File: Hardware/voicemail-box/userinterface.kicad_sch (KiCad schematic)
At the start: 5 parts, among them SW801 Push_Button

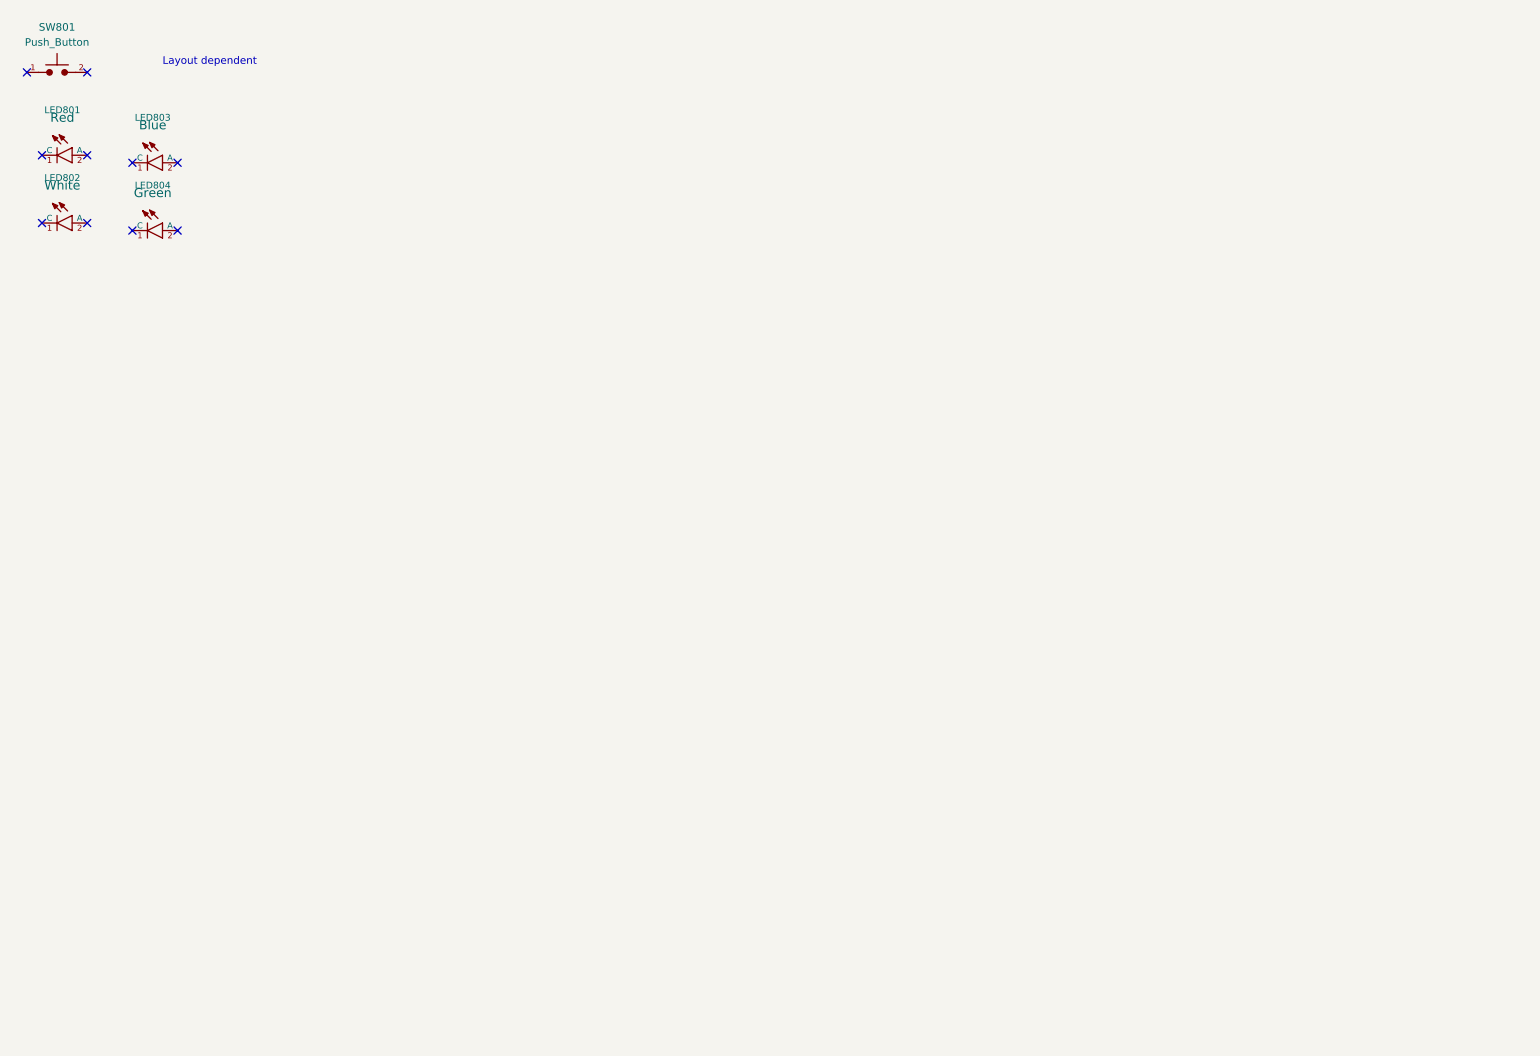
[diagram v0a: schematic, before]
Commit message: HW Layout progress todo: + Antenna + Audio Jacks + Planes (Supply only)
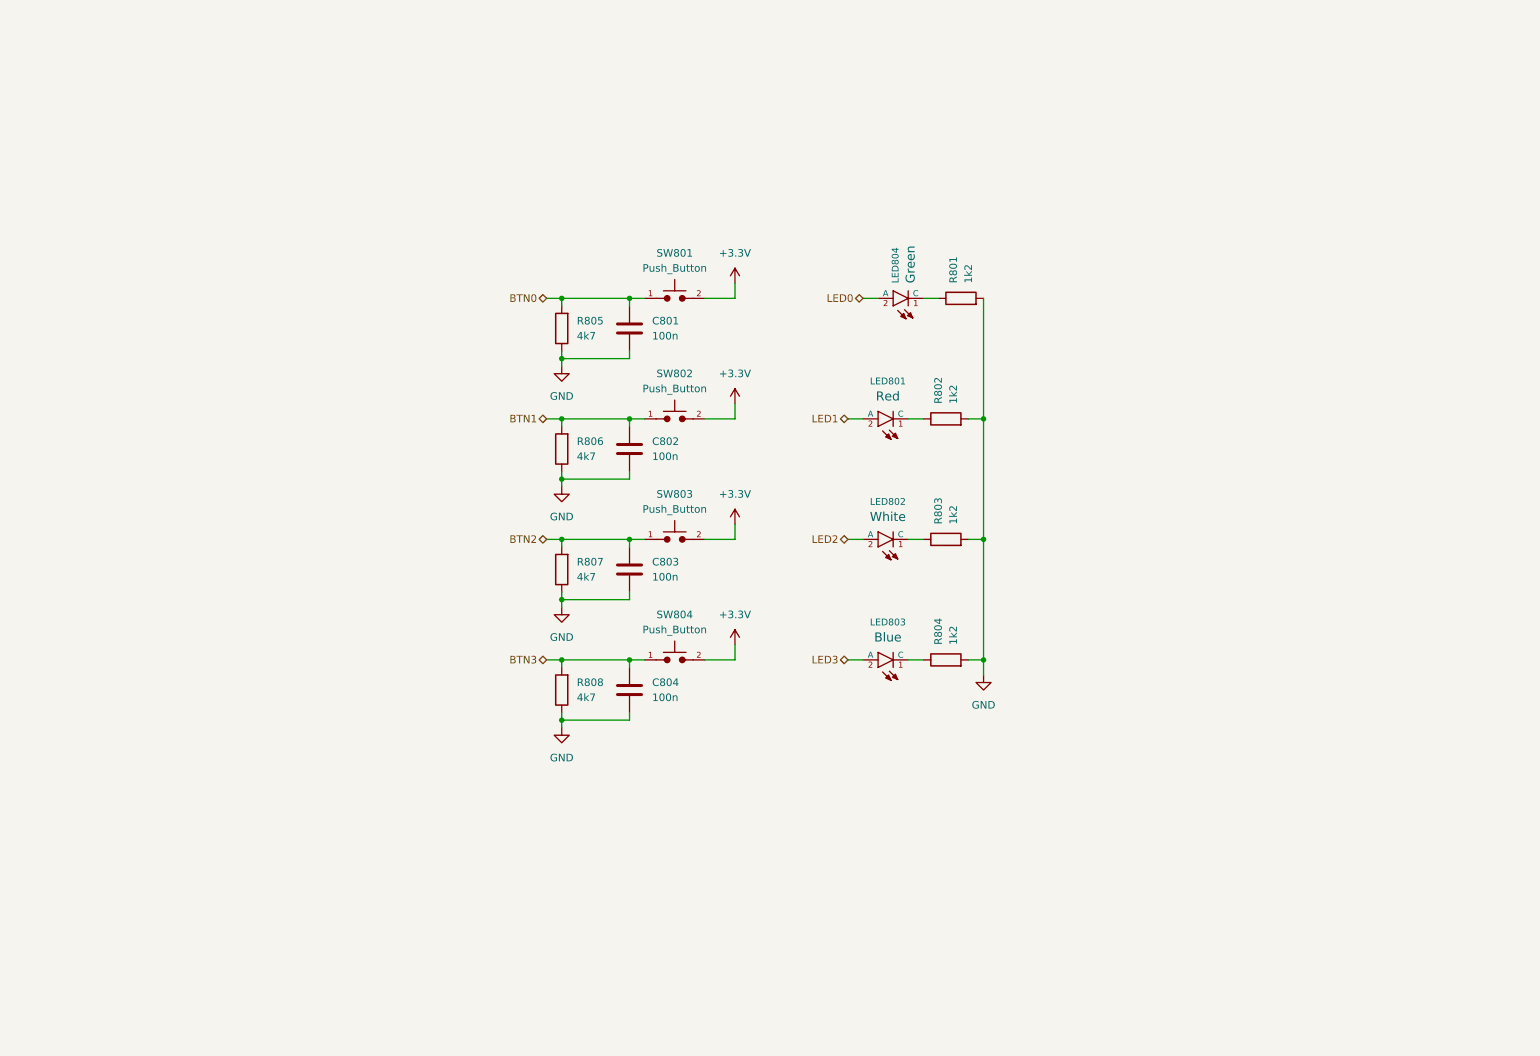
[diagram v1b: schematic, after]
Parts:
- added C801, C802, C803, C804: 100n, Capacitor_SMD:C_0603_1608Metric_Pad1.08x0.95mm_HandSolder, symbol Device:C
- added R801, R802, R803, R804: 1k2, Resistor_SMD:R_0603_1608Metric_Pad0.98x0.95mm_HandSolder, symbol Device:R
- added R805, R806, R807, R808: 4k7, Resistor_SMD:R_0603_1608Metric_Pad0.98x0.95mm_HandSolder, symbol Device:R
- added SW802, SW803, SW804: Push_Button, Button_Switch_THT:SW_PUSH_6mm, symbol PCM_SL_Devices:Push_Button
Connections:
- net BTN0: now reaches SW801.1
- net BTN0: now also C801.1, R805.2
- net +3.3V: now reaches SW801.2
- net +3.3V: now also SW802.2, SW803.2, SW804.2
- net at LED801.1 (C): now also R802.1
- net LED1: now reaches LED801.2 (A)
- net at LED802.1 (C): now also R803.1
- net LED2: now reaches LED802.2 (A)
- net at LED803.1 (C): now also R804.1
- net LED3: now reaches LED803.2 (A)
- net at LED804.1 (C): now also R801.1
- net LED0: now reaches LED804.2 (A)
- new net BTN1: C802.1, R806.2, SW802.1
- new net BTN2: C803.1, R807.2, SW803.1
- new net BTN3: C804.1, R808.2, SW804.1
- new net GND: C801.2, C802.2, C803.2, C804.2, R801.2, R802.2, R803.2, R804.2, R805.1, R806.1, R807.1, R808.1
- no-connect marks 10 -> 0
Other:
- note removed: "Layout dependent"
- moved on the sheet: LED801, LED802, LED803, LED804, SW801

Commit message: layout progress step
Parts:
- added J801: Conn_01x08, Connector_PinHeader_2.54mm:PinHeader_1x08_P2.54mm_Vertical, symbol Connector_Generic:Conn_01x08
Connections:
- net +3.3V: now also J801.1 (Pin_1)
- net BTN1: now also J801.2 (Pin_2)
- net BTN2: now also J801.4 (Pin_4)
- net BTN3: now also J801.6 (Pin_6)
- net GND: now also J801.8 (Pin_8)
- net LED1: now also J801.3 (Pin_3)
- net LED2: now also J801.5 (Pin_5)
- net LED3: now also J801.7 (Pin_7)
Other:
- moved on the sheet: C801, C802, C803, C804, LED801, LED802, LED803, LED804, R801, R802, R803, R804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

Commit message: schema review
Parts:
- removed LED802: White_min200mcd_0603, PCM_4ms_LED:LED_0603_1608Metric, symbol PCM_4ms_LED:White_min200mcd_0603
- removed LED803: Blue_56mcd_0603, PCM_4ms_LED:LED_0603_1608Metric, symbol PCM_4ms_LED:Blue_56mcd_0603
- removed R803, R804: 1k2, Resistor_SMD:R_0603_1608Metric_Pad0.98x0.95mm_HandSolder, symbol Device:R
- added C811: 100n, Capacitor_SMD:C_0603_1608Metric_Pad1.08x0.95mm_HandSolder, symbol Device:C
- added J802, J803: Conn_01x03, Connector_PinHeader_2.54mm:PinHeader_1x03_P2.54mm_Vertical, symbol Connector_Generic:Conn_01x03
- added R809, R810, R811, R812, R813, R814: 4k7, Resistor_SMD:R_0603_1608Metric_Pad0.98x0.95mm_HandSolder, symbol Device:R
- added RV801, RV802: potentiometer_RK163, Potentiometer_THT:Potentiometer_Alps_RK163_Single_Horizontal, symbol PCM_SL_Devices:potentiometer_RK163
- added U801: 74LS07, Package_SO:SOIC-14_3.9x8.7mm_P1.27mm, symbol 74xx:74LS07
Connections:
- net +3.3V: now also J802.1 (Pin_1), J803.1 (Pin_1), RV801.1, RV802.1; no longer J801.1 (Pin_1), SW801.2, SW802.2, SW803.2, SW804.2
- net BTN0: now also U801.6; no longer SW801.1
- net BTN1: now also U801.8; no longer J801.2 (Pin_2), SW802.1
- net BTN2: now also U801.10; no longer J801.4 (Pin_4), SW803.1
- net BTN3: now also U801.12; no longer J801.6 (Pin_6), SW804.1
- net GND: now also SW801.2, SW802.2, SW803.2, SW804.2, C811.2, J802.3 (Pin_3), J803.3 (Pin_3), R809.1, R810.1, RV801.3, RV802.3, U801.7 (GND); no longer R801.2, R802.2
- net LED0: now also R810.2, U801.1; no longer LED804.2 (A)
- net LED1: now also R809.2, U801.3; no longer J801.3 (Pin_3), LED801.2 (A)
- net LED2 renamed ext_BTN1
- net ext_BTN1: now also SW802.1, R811.1, U801.9
- net LED3 renamed ext_BTN3
- net ext_BTN3: now also SW804.1, R813.1, U801.13
- new net +5V: C811.1, J801.1 (Pin_1), LED801.2 (A), LED804.2 (A), R811.2, R812.2, R813.2, R814.2, U801.14 (VCC)
- new net POT1: J802.2 (Pin_2), RV801.2
- new net POT2: J803.2 (Pin_2), RV802.2
- new net ext_BTN0: J801.4 (Pin_4), R814.1, SW801.1, U801.5
- new net ext_BTN2: J801.6 (Pin_6), R812.1, SW803.1, U801.11
- new net ext_LED1: J801.2 (Pin_2), R801.2, U801.2
- new net ext_LED2: J801.3 (Pin_3), R802.2, U801.4
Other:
- moved on the sheet: J801, LED801, LED804, R801, R802, R805, R806, R807, R808, SW801, SW802, SW803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

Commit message: ~layout
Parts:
- removed C801, C802, C803, C804: 100n, Capacitor_SMD:C_0603_1608Metric_Pad1.08x0.95mm_HandSolder, symbol Device:C
- removed J802, J803: Conn_01x03, Connector_PinHeader_2.54mm:PinHeader_1x03_P2.54mm_Vertical, symbol Connector_Generic:Conn_01x03
- added C812, C813, C814, C815: 100n, Capacitor_SMD:C_0603_1608Metric_Pad1.08x0.95mm_HandSolder, symbol Device:C
- added J802, J803: Conn_02x03_Odd_Even, Connector_PinSocket_2.54mm:PinSocket_2x03_P2.54mm_Vertical, symbol Connector_Generic:Conn_02x03_Odd_Even
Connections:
- net ext_LED2 is gone; now on net ext_LED1: J801.3 (Pin_3), R802.2, U801.4
- net BTN0: now also R805.1; no longer R805.2
- net BTN1: now also R806.1; no longer R806.2
- net BTN2: now also R807.1; no longer R807.2
- net BTN3: now also R808.1; no longer R808.2
- net GND: now also C812.2, C813.2, C814.2, C815.2, J802.6 (Pin_6), J803.6 (Pin_6); no longer R805.1, R806.1, R807.1, R808.1
- net POT1: now also J803.3 (Pin_3); no longer RV801.2
- net ext_BTN0: now also C812.1
- net ext_BTN1: now also C813.1
- net ext_BTN2: now also C814.1
- net ext_BTN3: now also C815.1
- net ext_LED1: no longer J801.2 (Pin_2), R801.2, U801.2
- net +3.3V renamed +3V3
- net +3V3: now also R805.2, R807.2, R808.2, J802.2 (Pin_2), J803.2 (Pin_2)
- net POT2: no longer names the net of RV802.2
- net POT2: now also J803.1 (Pin_1)
- new net: J802.1 (Pin_1), RV801.2
- new net POT0: J802.3 (Pin_3)
- new net ext_LED0: J801.2 (Pin_2), R801.2, U801.2
- new net ext_Poti0: J802.4 (Pin_4), J802.5 (Pin_5)
- new net ext_Poti1: J803.4 (Pin_4), J803.5 (Pin_5)
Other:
- moved on the sheet: C811, J801, R805, R806, R807, R808, R811, R812, R813, R814, RV801, RV802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

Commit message: state of pcb ordered
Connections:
- net +3V3: now also R806.2
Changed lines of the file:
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@@
+	(wire
+		(pts
+			(xy 198.12 60.96) (xy 198.12 62.23)
+		)
+		(stroke
+			(width 0)
+			(type default)
+		)
+	)
 	(wire
 		(pts
